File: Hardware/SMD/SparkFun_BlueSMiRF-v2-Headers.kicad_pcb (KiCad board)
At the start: 2 copper layers, 38.1 x 15.2 mm, 57 parts, among them J1 Conn_01x06, Q1 NMOS_0.2A_50V, Q2 NMOS_0.2A_50V, SW1 SPST_Momentary_4.6x2.8mm, U1 ESP32-PICO-V3-02, U2 AP2112K-3.3

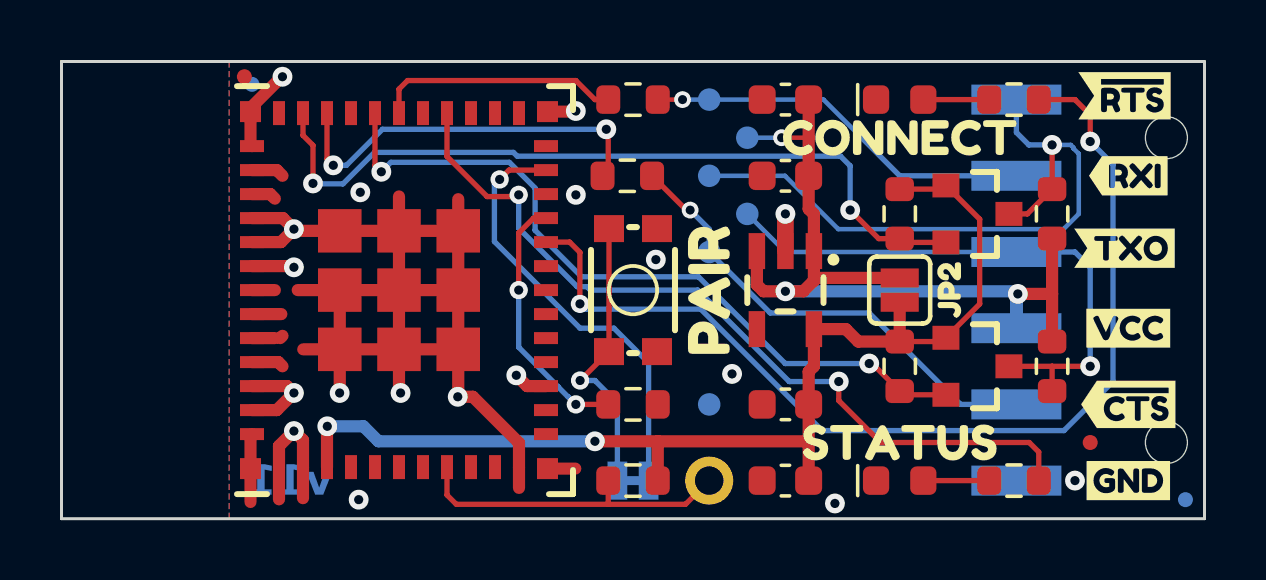
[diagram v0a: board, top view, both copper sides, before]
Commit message: Add 3D models
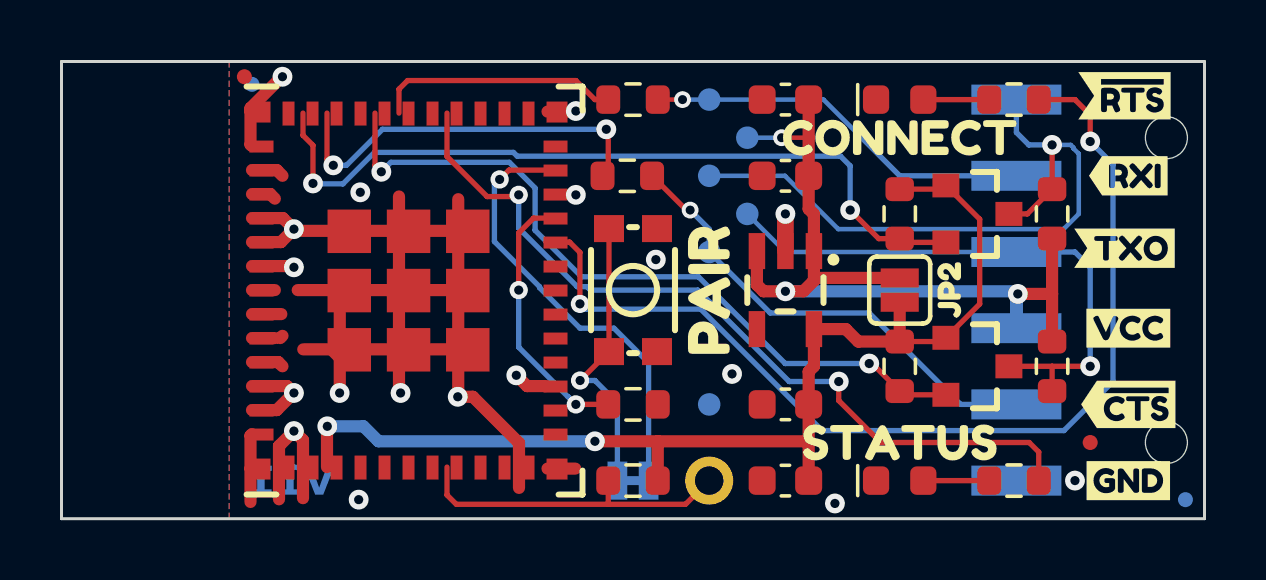
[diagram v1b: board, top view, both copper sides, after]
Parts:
- D1: footprint SparkFun-LED:LED_0603_1608Metric -> SparkFun-LED:LED_0603_1608Metric_Green
- D2: footprint SparkFun-LED:LED_0603_1608Metric -> SparkFun-LED:LED_0603_1608Metric_Red
- J1: footprint SparkFun-Connector:1X06-SMD_RA_MALE -> SparkFun-Connector:1x06_SMD_RA_Male
- JP1: footprint SparkFun-Jumper:SMT-JUMPER_2_NC_TRACE_SILK -> SparkFun-Jumper:Jumper_2_NC_Trace
- JP2: footprint SparkFun-Jumper:SMT-JUMPER_2_NO_SILK -> SparkFun-Jumper:Jumper_2_NO
- SW1: footprint SparkFun-Switch:Momentary_SMD_4.6x2.8mm -> SparkFun-Switch:Push_SMD_4.6x2.8mm_h2.5mm
- TP1: footprint SparkFun-Connector:1X01 -> SparkFun-Connector:1x01
- U1: footprint SparkFun-RF:ESP32-MINI -> SparkFun-RF:ESP32-PICO-MINI
- U3: footprint SparkFun-Aesthetic:ORDERING_INSTRUCTIONS -> SparkFun-Aesthetic:Ordering_Instructions
- moved U1 0.32 mm to (141.1, 124.5)
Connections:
- D1 pad 2: Net-(D1-A) -> unconnected-(D1-A-Pad2)
- D2 pad 2: Net-(D2-A) -> unconnected-(D2-A-Pad2)
- Q1 pad 1: +3.3V -> unconnected-(Q1-G-Pad1)
- Q2 pad 1: +3.3V -> unconnected-(Q2-G-Pad1)
- R2 pad 1: Net-(U1-IOA15) -> unconnected-(R2-Pad1)
- R2 pad 2: GND -> unconnected-(R2-Pad2)
- R3 pad 1: RX_LV -> unconnected-(R3-Pad1)
- R3 pad 2: RX_HV -> unconnected-(R3-Pad2)
- R4 pad 1: ~{CTS_LV} -> unconnected-(R4-Pad1)
- R4 pad 2: ~{CTS_HV} -> unconnected-(R4-Pad2)
- R5 pad 1: /Connect -> unconnected-(R5-Pad1)
- R5 pad 2: Net-(D1-A) -> unconnected-(R5-Pad2)
- R6 pad 1: /Status -> unconnected-(R6-Pad1)
- R6 pad 2: Net-(D2-A) -> unconnected-(R6-Pad2)
- U1 pad 21: Net-(U1-IOA15) -> unconnected-(U1-IOA15-Pad21)
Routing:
- net unconnected-(R5-Pad1): track 0.00 -> 34.3 mm, vias 0 -> 2
- net /Connect: track 34.3 -> 0.00 mm, vias 2 -> 0
- net unconnected-(R6-Pad1): track 0.00 -> 27.3 mm, vias 0 -> 2
- net /Status: track 27.3 -> 0.00 mm, vias 2 -> 0
- net ~{CTS_LV}: track 13.0 -> 0.00 mm, vias 2 -> 0
- net unconnected-(R4-Pad1): track 0.00 -> 13.0 mm, vias 0 -> 2
- net unconnected-(R2-Pad1): track 0.00 -> 8.70 mm, vias 0 -> 2
- net Net-(U1-IOA15): track 8.70 -> 0.00 mm, vias 2 -> 0
- net unconnected-(R3-Pad1): track 0.00 -> 8.16 mm
- net RX_LV: track 8.16 -> 0.00 mm
- net (no net): track 0.00 -> 4.39 mm
- net Net-(D2-A): track 2.20 -> 0.00 mm
- net Net-(D1-A): track 2.20 -> 0.00 mm
- net unconnected-(U1-IOA2-Pad22): vias 0 -> 1
- net unconnected-(U1-IA34-Pad9): vias 0 -> 1
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
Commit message: Revert "Add 3D models"
This reverts commit f06ec004f059f8b2f723d6c27b798dd6a6ac20d5.
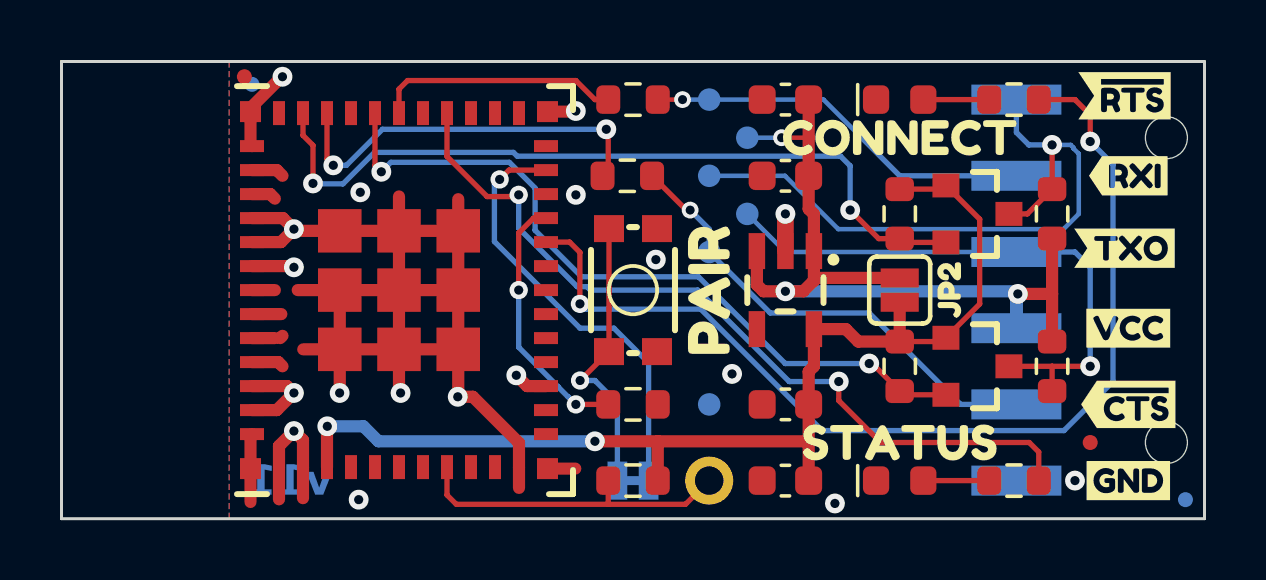
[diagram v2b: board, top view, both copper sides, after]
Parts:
- D1: footprint SparkFun-LED:LED_0603_1608Metric_Green -> SparkFun-LED:LED_0603_1608Metric
- D2: footprint SparkFun-LED:LED_0603_1608Metric_Red -> SparkFun-LED:LED_0603_1608Metric
- J1: footprint SparkFun-Connector:1x06_SMD_RA_Male -> SparkFun-Connector:1X06-SMD_RA_MALE
- JP1: footprint SparkFun-Jumper:Jumper_2_NC_Trace -> SparkFun-Jumper:SMT-JUMPER_2_NC_TRACE_SILK
- JP2: footprint SparkFun-Jumper:Jumper_2_NO -> SparkFun-Jumper:SMT-JUMPER_2_NO_SILK
- SW1: footprint SparkFun-Switch:Push_SMD_4.6x2.8mm_h2.5mm -> SparkFun-Switch:Momentary_SMD_4.6x2.8mm
- TP1: footprint SparkFun-Connector:1x01 -> SparkFun-Connector:1X01
- U1: footprint SparkFun-RF:ESP32-PICO-MINI -> SparkFun-RF:ESP32-MINI
- U3: footprint SparkFun-Aesthetic:Ordering_Instructions -> SparkFun-Aesthetic:ORDERING_INSTRUCTIONS
- moved U1 0.32 mm to (140.8, 124.5)
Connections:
- D1 pad 2: unconnected-(D1-A-Pad2) -> Net-(D1-A)
- D2 pad 2: unconnected-(D2-A-Pad2) -> Net-(D2-A)
- Q1 pad 1: unconnected-(Q1-G-Pad1) -> +3.3V
- Q2 pad 1: unconnected-(Q2-G-Pad1) -> +3.3V
- R2 pad 1: unconnected-(R2-Pad1) -> Net-(U1-IOA15)
- R2 pad 2: unconnected-(R2-Pad2) -> GND
- R3 pad 1: unconnected-(R3-Pad1) -> RX_LV
- R3 pad 2: unconnected-(R3-Pad2) -> RX_HV
- R4 pad 1: unconnected-(R4-Pad1) -> ~{CTS_LV}
- R4 pad 2: unconnected-(R4-Pad2) -> ~{CTS_HV}
- R5 pad 1: unconnected-(R5-Pad1) -> /Connect
- R5 pad 2: unconnected-(R5-Pad2) -> Net-(D1-A)
- R6 pad 1: unconnected-(R6-Pad1) -> /Status
- R6 pad 2: unconnected-(R6-Pad2) -> Net-(D2-A)
- U1 pad 21: unconnected-(U1-IOA15-Pad21) -> Net-(U1-IOA15)
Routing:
- net unconnected-(R5-Pad1): track 34.3 -> 0.00 mm, vias 2 -> 0
- net /Connect: track 0.00 -> 34.3 mm, vias 0 -> 2
- net unconnected-(R6-Pad1): track 27.3 -> 0.00 mm, vias 2 -> 0
- net /Status: track 0.00 -> 27.3 mm, vias 0 -> 2
- net ~{CTS_LV}: track 0.00 -> 13.0 mm, vias 0 -> 2
- net unconnected-(R4-Pad1): track 13.0 -> 0.00 mm, vias 2 -> 0
- net unconnected-(R2-Pad1): track 8.70 -> 0.00 mm, vias 2 -> 0
- net Net-(U1-IOA15): track 0.00 -> 8.70 mm, vias 0 -> 2
- net unconnected-(R3-Pad1): track 8.16 -> 0.00 mm
- net RX_LV: track 0.00 -> 8.16 mm
- net (no net): track 4.39 -> 0.00 mm
- net Net-(D2-A): track 0.00 -> 2.20 mm
- net Net-(D1-A): track 0.00 -> 2.20 mm
- net unconnected-(U1-IOA2-Pad22): vias 1 -> 0
- net unconnected-(U1-IA34-Pad9): vias 1 -> 0
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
